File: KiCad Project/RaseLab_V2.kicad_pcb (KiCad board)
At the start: 2 copper layers, 95 x 54.8 mm, 50 parts, among them IC1 LT8607EMSE#TRPBF, J1 Conn_02x04_Odd_Even_modifié, J3 Conn_01x08_Pin, J4 Screw_Terminal_01x03, J5 TYPE-C-31-M-12, SW1 SW_Push, SW2 SW_Push, U2 ESP32-S3-MINI-1

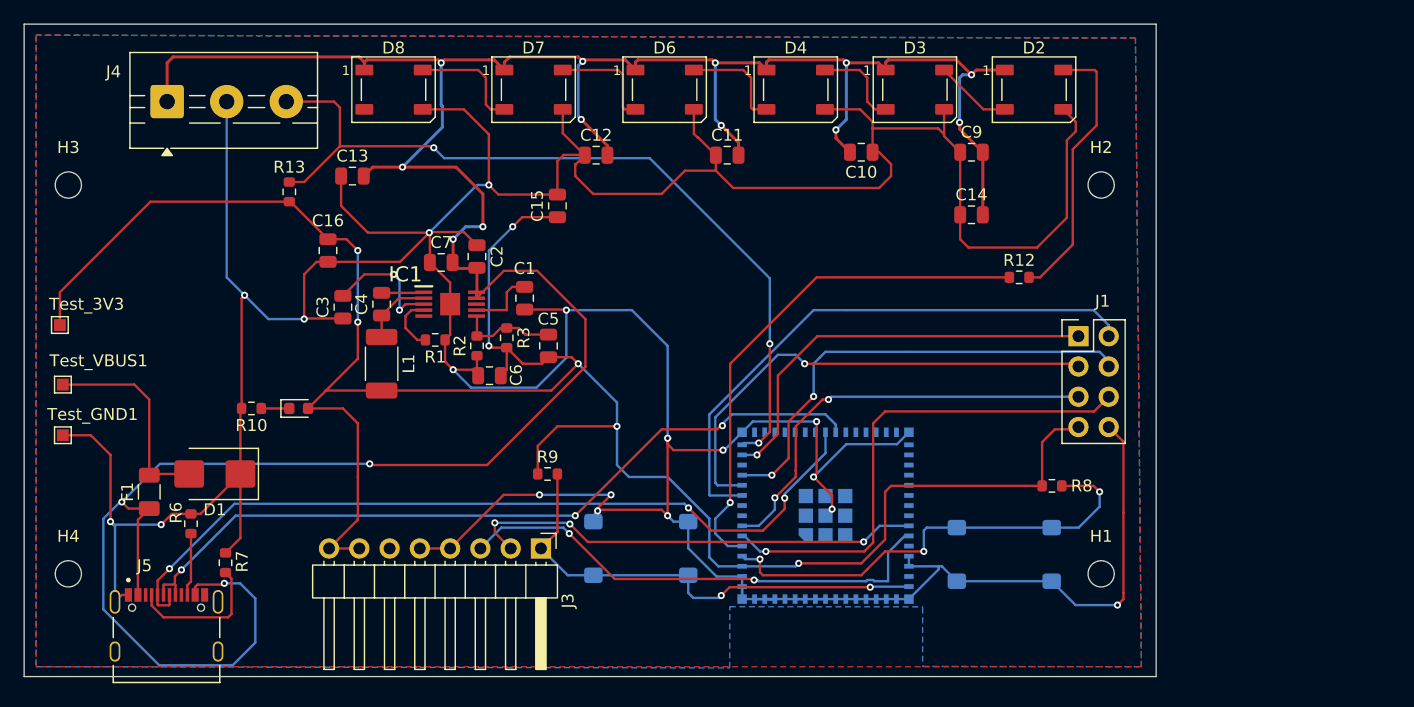
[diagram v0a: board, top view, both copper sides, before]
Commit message: feat(kicad): add name to component card
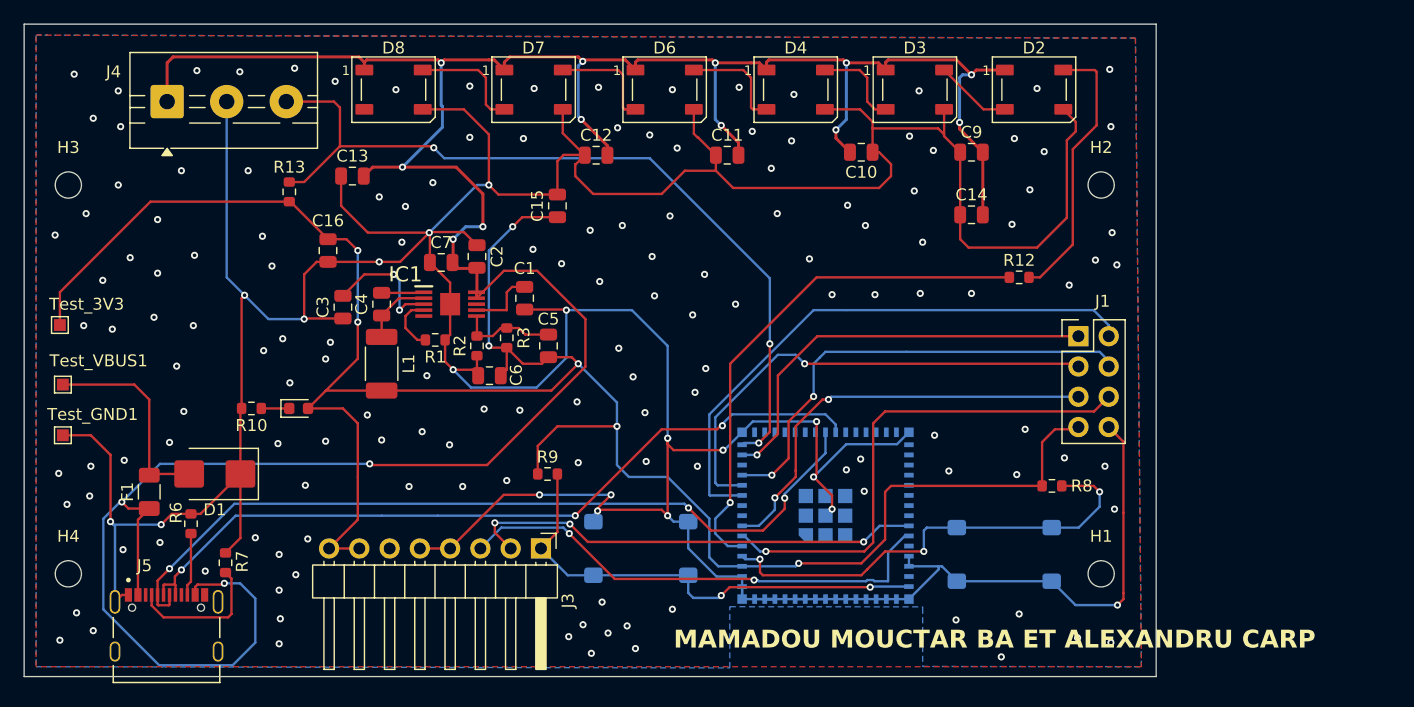
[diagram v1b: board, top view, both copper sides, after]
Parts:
- L1: value 2.2µF -> 2.2µH
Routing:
- net GND: vias 18 -> 168
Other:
- board text added: "CAMPUS FAB"
- board text added: "MAMADOU MOUCTAR BA ET ALEXANDRU CARP"

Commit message: RECTIFATION DE CERTAINS ERREURS
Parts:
- C1, C10, C11, C12, C13, C14, C15, C16, C2, C3, C4, C5, C6, C7, C9: footprint Capacitor_SMD:C_0805_2012Metric -> Capacitor_SMD:C_0603_1608Metric
- D1: footprint Diode_SMD:D_SMB -> Diode_SMD:D_SOD-123
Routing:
- net GND: track 419.1 -> 417.8 mm
- net Net-(D1-A2): track 17.5 -> 18.3 mm

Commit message: AJOUT DES NONS SUR LES CONNECTEURS EXTERNES
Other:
- board text added: "3V3"
- board text added: "BUSY"
- board text added: "CS"
- board text added: "D/C"
- board text added: "GND"
- board text added: "GPIO11"
- board text added: "NON CONNECTE"
- board text added: "RES"
- board text added: "REST"
- board text added: "RXD0"
- board text added: "SDA"
- board text added: "SLC"
- board text added: "TXD0"
- board text added: "VBUS"
- board text added: "VCC"
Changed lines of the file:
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@@
 		(layer "Edge.Cuts")
+	)
+	(gr_text "VBUS\n"
+		(at 57.5 45.7 0)
+		(layer "F.SilkS")
+		(effects
+			(font
+				(size 0.8 0.5)
+				(thickness 0.1)
+			)
+			(justify left bottom)
+		)
+	)
+	(gr_text "GND\n"
+		(at 62.6 45.6 0)
+		(layer "F.SilkS")
+		(effects
+			(font
+				(size 0.8 0.5)
+				(thickness 0.1)
+			)
+			(justify left bottom)
+		)
+	)
+	(gr_text "GPIO11\n"
+		(at 67.2 45.7 0)
+		(layer "F.SilkS")
+		(effects
+			(font
+				(size 0.8 0.5)
+				(thickness 0.1)
+			)
+			(justify left bottom)
+		)
+	)
+	(gr_text "3V3\n"
+		(at 71.3 78.6 0)
+		(layer "F.SilkS")
+		(effects
+			(font
+				(size 0.8 0.5)
+				(thickness 0.1)
+			)
+			(justify left bottom)
+		)
+	)
+	(gr_text "3V3\n"
+		(at 73.7 78.7 0)
+		(layer "F.SilkS")
+		(effects
+			(font
+				(size 0.8 0.5)
+				(thickness 0.1)
+			)
+			(justify left bottom)
+		)
+	)
+	(gr_text "NON\nCONNECTE\n\n"
+		(at 75.5 80 0)
+		(layer "F.SilkS")
+		(effects
+			(font
+				(size 0.8 0.5)
+				(thickness 0.1)
+			)
+			(justify left bottom)
+		)
+	)
+	(gr_text "GND\n"
+		(at 79.4 78.9 0)
+		(layer "F.SilkS")
+		(effects
+			(font
+				(size 0.8 0.5)
+				(thickness 0.1)
+			)
+			(justify left bottom)
+		)
+	)
+	(gr_text "GND\n"
+		(at 81.7 78.9 0)
+		(layer "F.SilkS")
+		(effects
+			(font
+				(size 0.8 0.5)
+				(thickness 0.1)
+			)
+			(justify left bottom)
+		)
+	)
+	(gr_text "RXD0\n"
+		(at 83.8 79 0)
+		(layer "F.SilkS")
+		(effects
+			(font
+				(size 0.8 0.5)
+				(thickness 0.1)
+			)
+			(justify left bottom)
+		)
+	)
+	(gr_text "TXD0\n"
+		(at 86.4 78.8 0)
+		(layer "F.SilkS")
+		(effects
+			(font
+				(size 0.8 0.5)
+				(thickness 0.1)
+			)
+			(justify left bottom)
+		)
+	)
+	(gr_text "REST\n"
+		(at 88.9 78.6 0)
+		(layer "F.SilkS")
+		(effects
+			(font
+				(size 0.8 0.5)
+				(thickness 0.1)
+			)
+			(justify left bottom)
+		)
+	)
+	(gr_text "SLC\n"
+		(at 133 67.9 90)
+		(layer "F.SilkS")
+		(effects
+			(font
+				(size 0.8 0.5)
+				(thickness 0.1)
+			)
+			(justify left bottom)
+		)
+	)
+	(gr_text "GND\n"
+		(at 133 70.5 90)
+		(layer "F.SilkS")
+		(effects
+			(font
+				(size 0.8 0.5)
+				(thickness 0.1)
+			)
+			(justify left bottom)
+		)
+	)
+	(gr_text "D/C\n"
+		(at 133.1 65.3 90)
+		(layer "F.SilkS")
+		(effects
+			(font
+				(size 0.8 0.5)
+				(thickness 0.1)
+			)
+			(justify left bottom)
+		)
+	)
+	(gr_text "BUSY\n"
+		(at 133.205 62.7 90)
+		(layer "F.SilkS")
+		(effects
+			(font
+				(size 0.8 0.5)
+				(thickness 0.1)
+			)
+			(justify left bottom)
+		)
+	)
+	(gr_text "RES\n"
+		(at 140 62.5 90)
+		(layer "F.SilkS")
+		(effects
+			(font
+				(size 0.8 0.5)
+				(thickness 0.1)
+			)
+			(justify left bottom)
+		)
+	)
+	(gr_text "CS\n"
+		(at 140 65.2 90)
+		(layer "F.SilkS")
+		(effects
+			(font
+				(size 0.8 0.5)
+				(thickness 0.1)
+			)
+			(justify left bottom)
+		)
+	)
+	(gr_text "SDA\n"
+		(at 140 68.1 90)
+		(layer "F.SilkS")
+		(effects
+			(font
+				(size 0.8 0.5)
+				(thickness 0.1)
+			)
+			(justify left bottom)
+		)
+	)
+	(gr_text "VCC\n"
+		(at 140 70.9 90)
+		(layer "F.SilkS")
+		(effects
+			(font
+				(size 0.8 0.5)
+				(thickness 0.1)
+			)
+			(justify left bottom)
+		)
 	)
 	(gr_text "MAMADOU MOUCTAR BA ET ALEXANDRU CARP\n"
